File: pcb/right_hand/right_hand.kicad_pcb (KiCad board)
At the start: 2 copper layers, 160 x 110 mm, 113 parts, among them J0 UJ20-C-H-G-SMT-P16-TR, U0 SW_Push

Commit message: Update right hand metadata
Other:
- board text added: "Stenoswitch Right Hand v0.3"
- board text removed: "Stenoswitch Right Hand v0.2"
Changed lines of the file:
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@@
 	(title_block
 		(title "Stenoswitch Right Hand")
-		(date "2025-09-05")
-		(rev "v0.2")
+		(date "2025-10-20")
+		(rev "v0.3")
 		(company "https://github.com/Bennett-Petzold/stenoswitch")
 		(comment 1 "NO WARRANTY. See license.")
@@
 		(layer "Edge.Cuts")
 	)
-	(gr_text "Stenoswitch Right Hand v0.2"
+	(gr_text "Stenoswitch Right Hand v0.3"
 		(at 184.2 57.6 0)
 		(layer "F.SilkS")
@@
 		)
 	)
-	(gr_text "Stenoswitch Right Hand v0.2"
+	(gr_text "Stenoswitch Right Hand v0.3"
 		(at 83.8 143.2 0)
 		(layer "F.SilkS")
@@
 		)
 	)
-	(gr_text "Stenoswitch Right Hand v0.2"
+	(gr_text "Stenoswitch Right Hand v0.3"
 		(at 111.35 145.32 0)
 		(layer "B.SilkS")
@@
 		)
 	)
-	(gr_text "Stenoswitch Right Hand v0.2"
+	(gr_text "Stenoswitch Right Hand v0.3"
 		(at 228.2 60.8 0)
 		(layer "B.SilkS")

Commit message: Readjust positive data ESD
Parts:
- moved CR1 4.31 mm to (73.6, 130.7)
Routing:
- net GND: vias 60 -> 59
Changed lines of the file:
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@@
 	(footprint "ultra_librarian_footprints:SOT5x3_DYA_TEX"
 		(layer "B.Cu")
-		(at 70.6 127.5493 -90)
+		(at 73.6 130.6507 -90)
 		(tags "ESD321DYAR ")
 		(property "Reference" "CR1"
@@
 			(polygon
 				(pts
-					(xy 70.2317 127.1556) (xy 70.2317 127.943) (xy 70.9683 127.943) (xy 70.9683 127.1556)
+					(xy 73.2317 130.257) (xy 73.2317 131.0444) (xy 73.9683 131.0444) (xy 73.9683 130.257)
 				)
 			)
@@
 	)
 	(via
-		(at 75.6 38.6)
-		(size 1.2)
-		(drill 0.6)
-		(layers "F.Cu" "B.Cu")
-		(free yes)
-		(net 15)
-	)
-	(via
 		(at 151.2 98.4)
 		(size 1.2)
@@
 	)
 	(segment
-		(start 70.6 126.8)
-		(end 70.5 126.7)
+		(start 73.6 129.9014)
+		(end 73.5 129.8014)
 		(width 0.5)
 		(layer "B.Cu")
@@
 	)
 	(segment
-		(start 70.5 126.7)
-		(end 70.5 125.94994)
+		(start 73.5 129.8014)
+		(end 73.5 129.05134)
 		(width 0.5)
 		(layer "B.Cu")
@@
 			)
 		)
+	)
+	(zone
+		(net 0)
+		(net_name "")
+		(layer "B.Cu")
+		(hatch edge 0.5)
+		(connect_pads
+			(clearance 0)
+		)
+		(min_thickness 0.25)
+		(filled_areas_thickness no)
+		(keepout
+			(tracks allowed)
+			(vias allowed)
+			(pads allowed)
+			(copperpour not_allowed)
+			(footprints allowed)
+		)
+		(placement
+			(enabled no)
+			(sheetname "")
+		)
+		(fill
+			(thermal_gap 0.5)
+			(thermal_bridge_width 0.5)
+		)
+		(polygon
+			(pts
+				(xy 100.4 38.8) (xy 100.4 37.2) (xy 98.8 37.2) (xy 98.8 38.6)
+			)
+		)

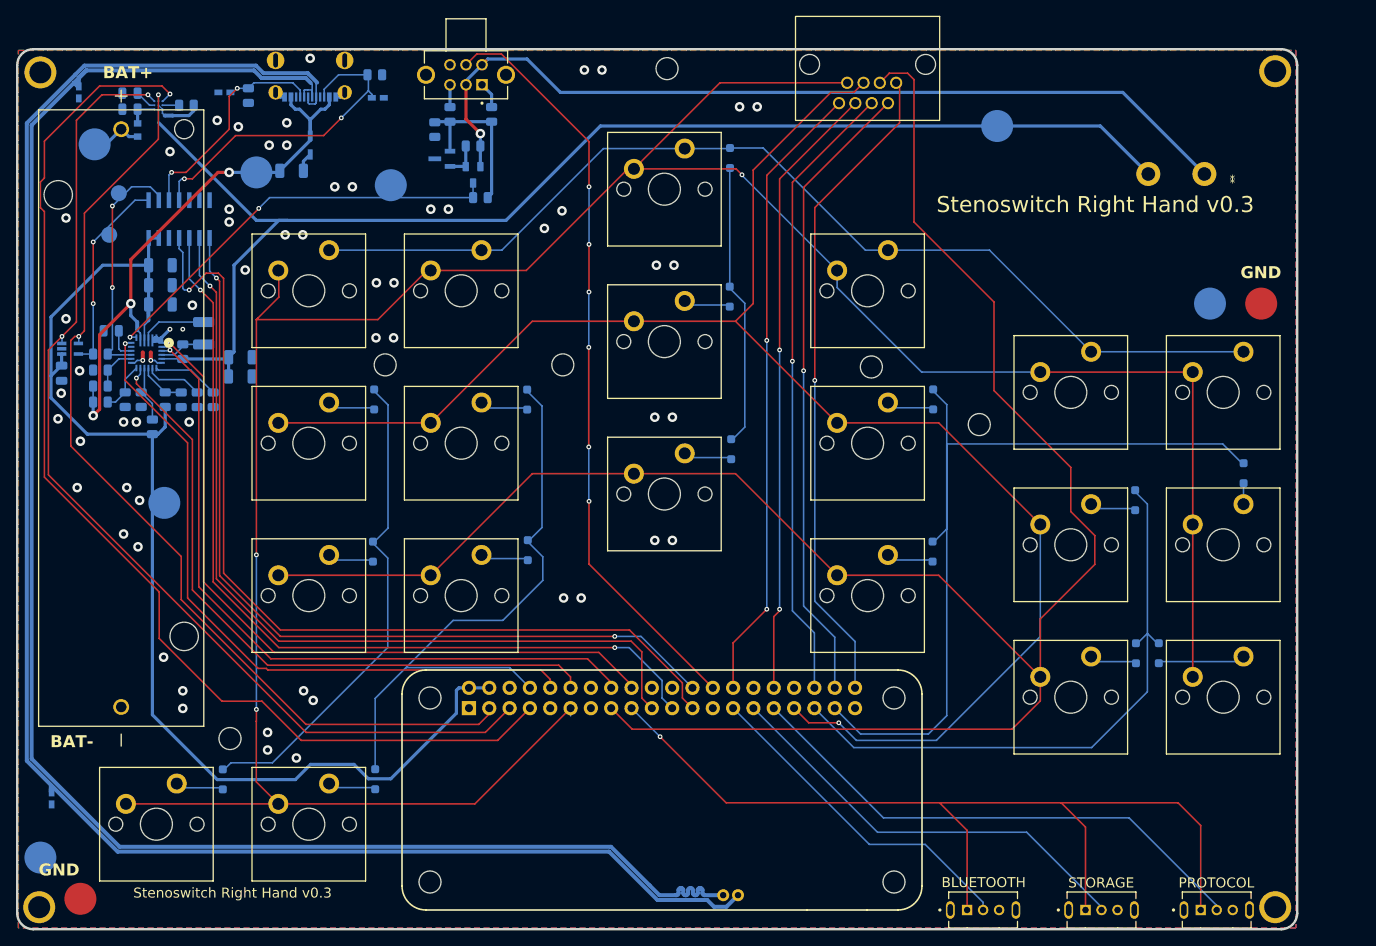
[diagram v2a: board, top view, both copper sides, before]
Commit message: Add more ESD protection
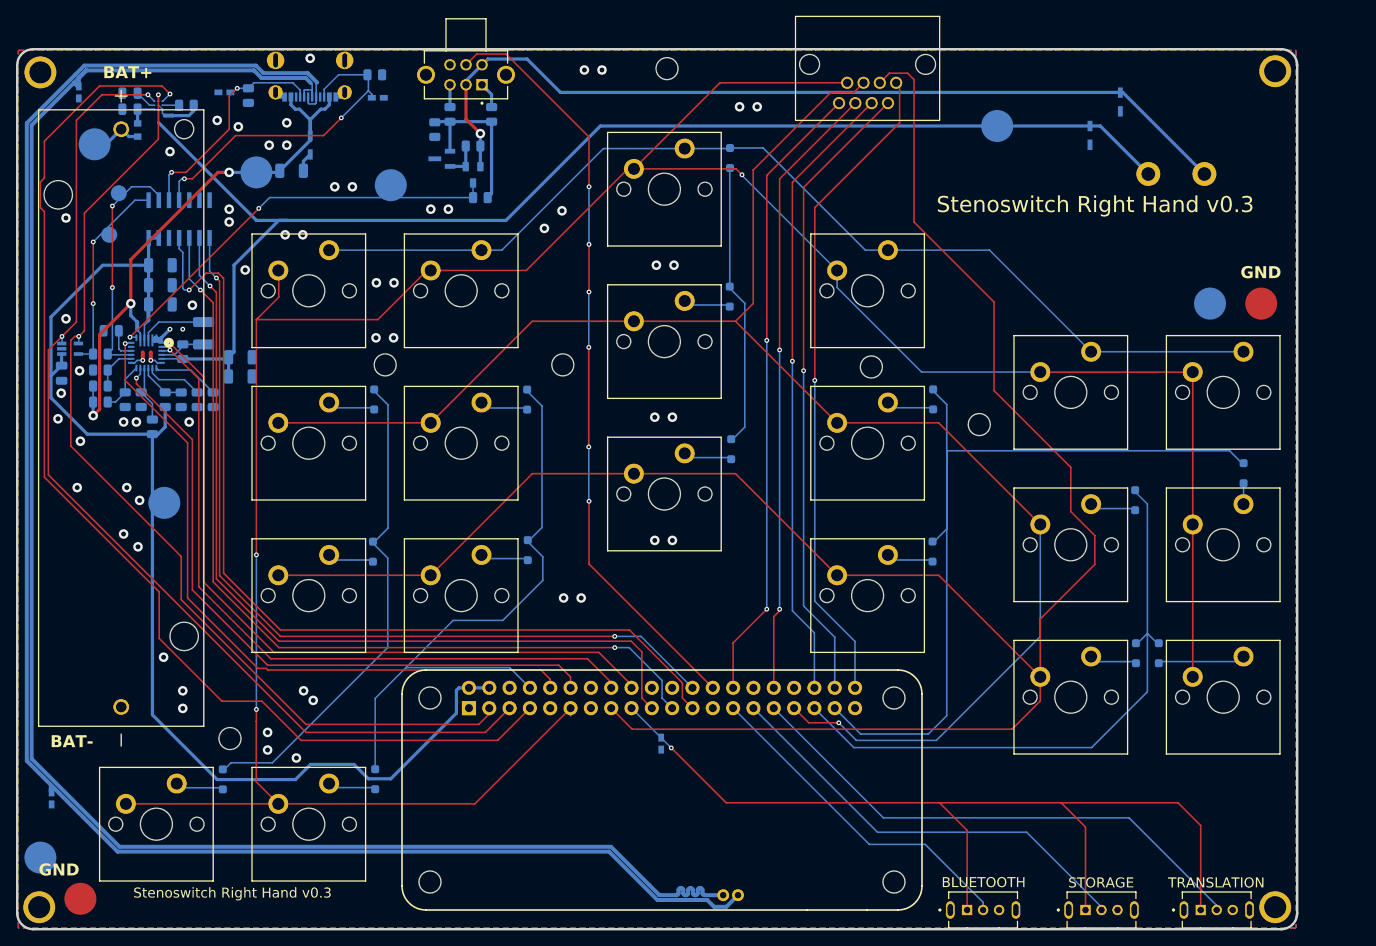
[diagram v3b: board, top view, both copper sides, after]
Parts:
- added CR5: ESD321DYAR, ultra_librarian_footprints:SOT5x3_DYA_TEX, B.Cu at (149.8, 123.8)
- added TSD05: TSD05DYFR, ultra_librarian_footprints:TVS_SOD2_DYF_TEX, B.Cu at (207.2, 43.6)
- added TSD05: TSD05DYFR, ultra_librarian_footprints:TVS_SOD2_DYF_TEX, B.Cu at (203.4, 47.8)
- CR1, CR4: value ESD321 -> ESD321DYAR
- CR2: value TSD05 -> TSD05DYFR
- C_{SYS}1: value 22uF(3) -> 22uF
- RFB_{H}0: value 31.6K -> 31.6k
- RLIM_{H}0: value 10K -> 10k
- RLIM_{L}0: value MCP40D19T -> MCP40D19T-104E_LT
- RNTC_{L}0: value 10K(2) -> 10k
- RREG_{H}0: value 15K -> 15k
- RWIN_{H}0: value 21.5K -> 21.5k
- RWIN_{L}0: value 5.1K -> 5.1k
- R_{ISET}0: value 73.2K -> 73.2k
- R_{OLIM}0: value 590K -> 590k
- R_{Store}0: value 8.06K -> 8.06k
- renumbered BAT_STORE to STORE_EN0, PROTOCOL to TRANSLATION
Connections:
- BLUETOOTH pad SH1: (no net) -> GND
- BLUETOOTH pad SH2: (no net) -> GND
- STORAGE pad SH1: (no net) -> GND
- STORAGE pad SH2: (no net) -> GND
- STORE_EN0 pad 6: unconnected-(STORE_EN0-Pad6) -> GND
- TRANSLATION pad SH1: (no net) -> GND
- TRANSLATION pad SH2: (no net) -> GND
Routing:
- net /Control/Right_Columns1: track 108.9 -> 107.7 mm
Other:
- board text added: "ESD321"
- board text added: "Fuse"

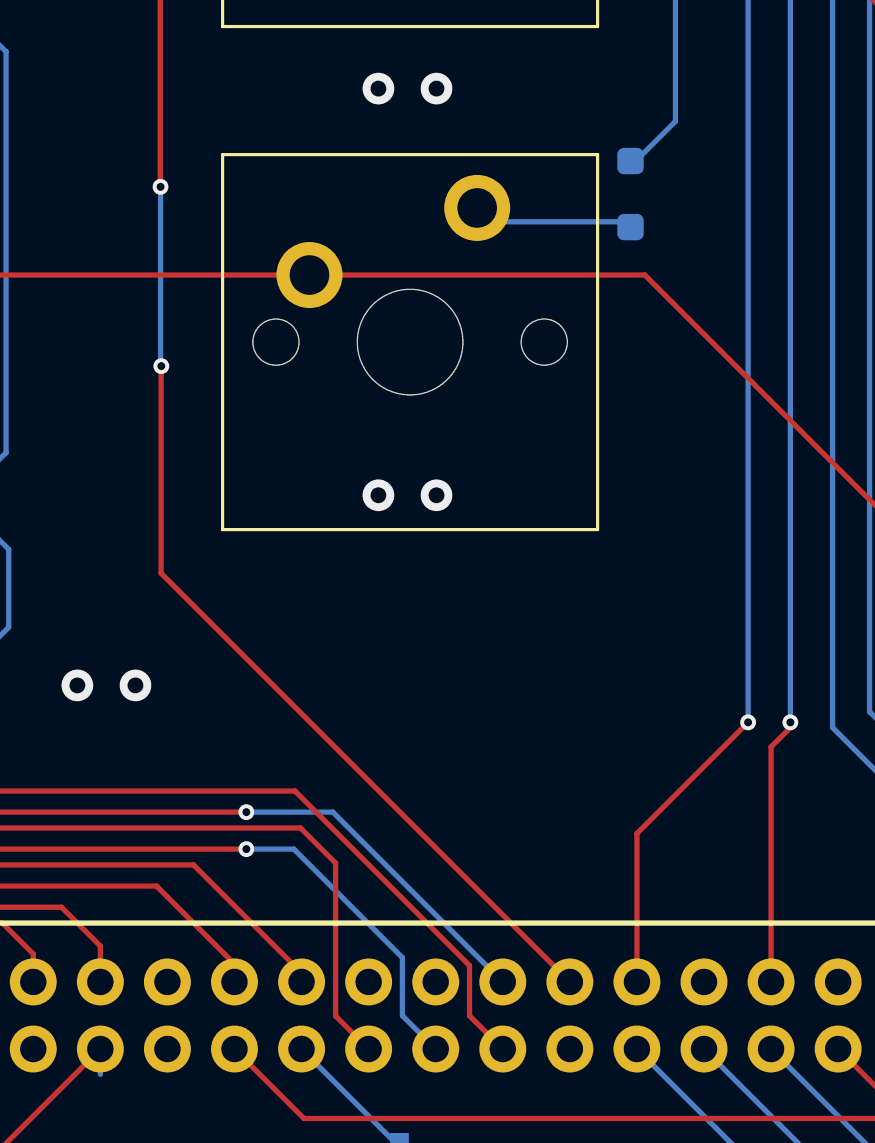
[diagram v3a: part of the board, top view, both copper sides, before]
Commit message: Connect right_columns 2 to RPi
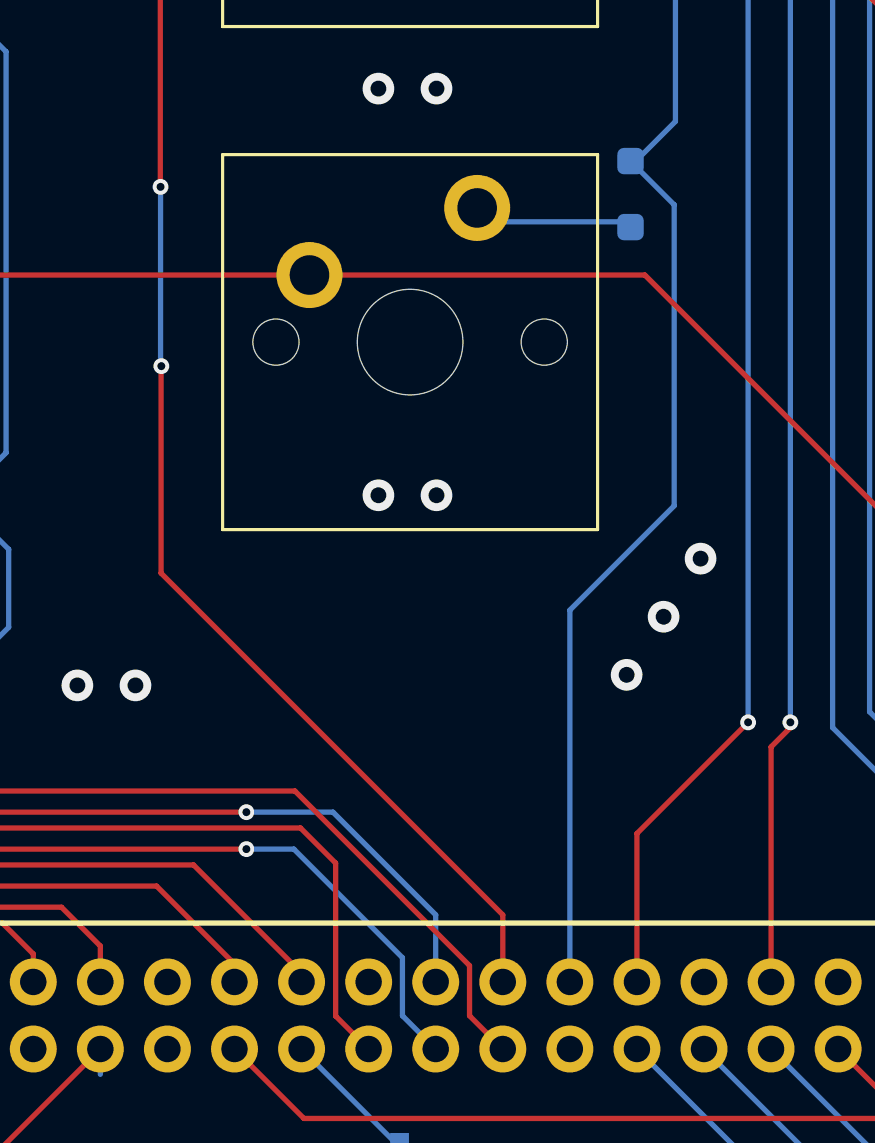
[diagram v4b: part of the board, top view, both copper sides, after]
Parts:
- BAT_MIN0: value DMG2305 -> DMG2305UX-7
- CR3: value ESD321 -> ESD321DYAR
- VBAT_PASS0: value TLV431 -> TLV431BIDBZR
- renumbered TSD05 to CR6, TSD05 to CR7
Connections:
- A1 pad 22: unconnected-(A1-GP25-Pad22) -> /Control/CS_{CURRENT}
- A1 pad 24: /Control/CS_{CURRENT} -> /Control/STORE_{ON}
- A1 pad 26: /Control/STORE_{ON} -> /Control/Right_Columns2
- BLUETOOTH pad SH1: GND -> (no net)
- BLUETOOTH pad SH2: GND -> (no net)
- STORAGE pad SH1: GND -> (no net)
- STORAGE pad SH2: GND -> (no net)
- TRANSLATION pad SH1: GND -> (no net)
- TRANSLATION pad SH2: GND -> (no net)
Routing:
- net /Control/Right_Columns2: track 35.4 -> 68.8 mm
- net /Control/CS_{CURRENT}: track 107.6 -> 106.6 mm
- net /Control/STORE_{ON}: track 95.5 -> 94.5 mm
- net GND: vias 59 -> 62

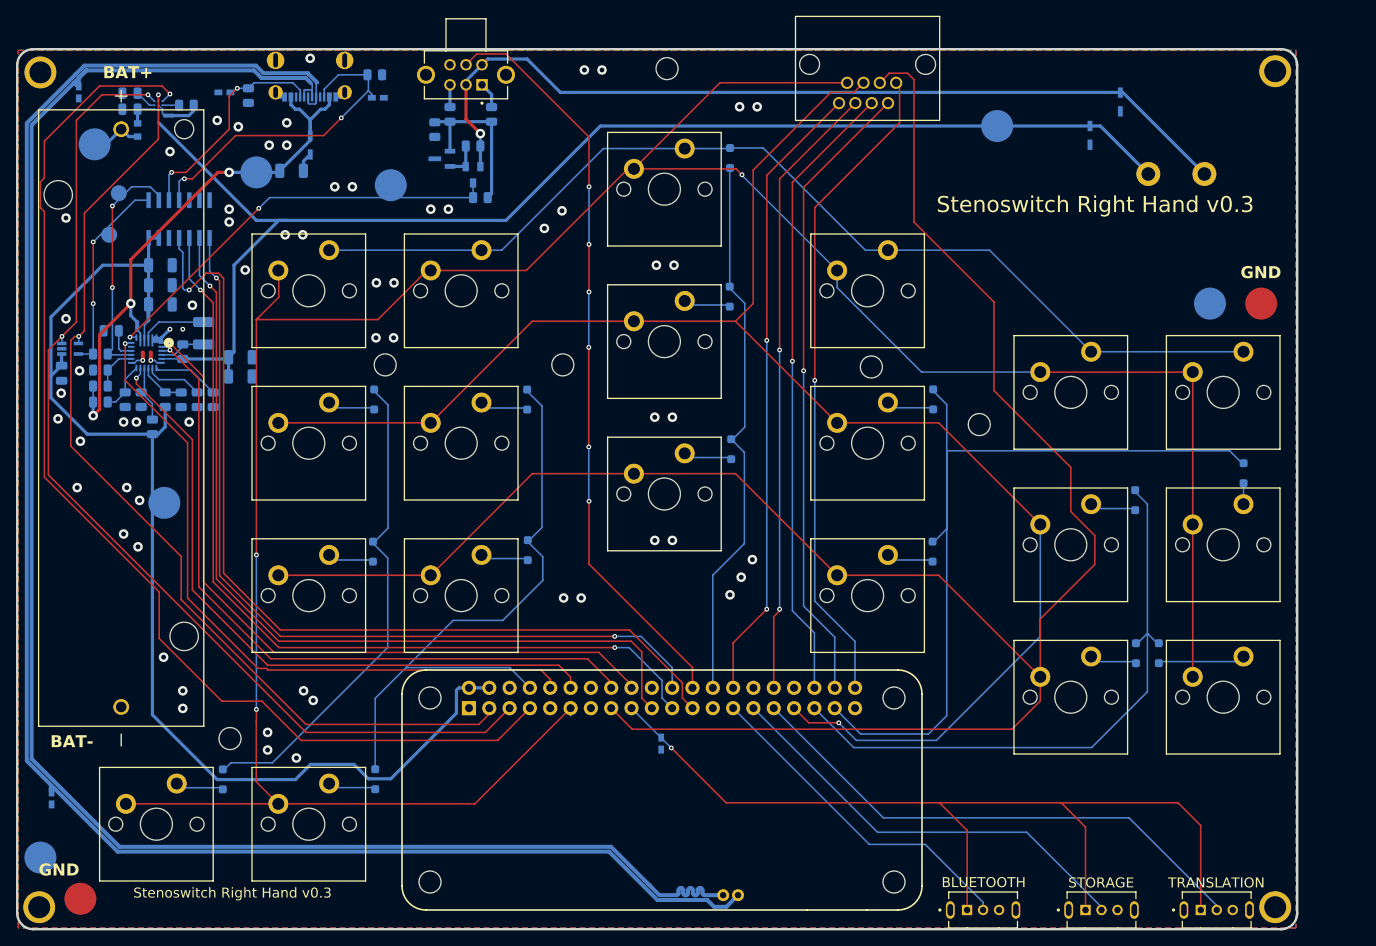
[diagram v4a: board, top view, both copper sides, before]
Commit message: Ground right hand through holes
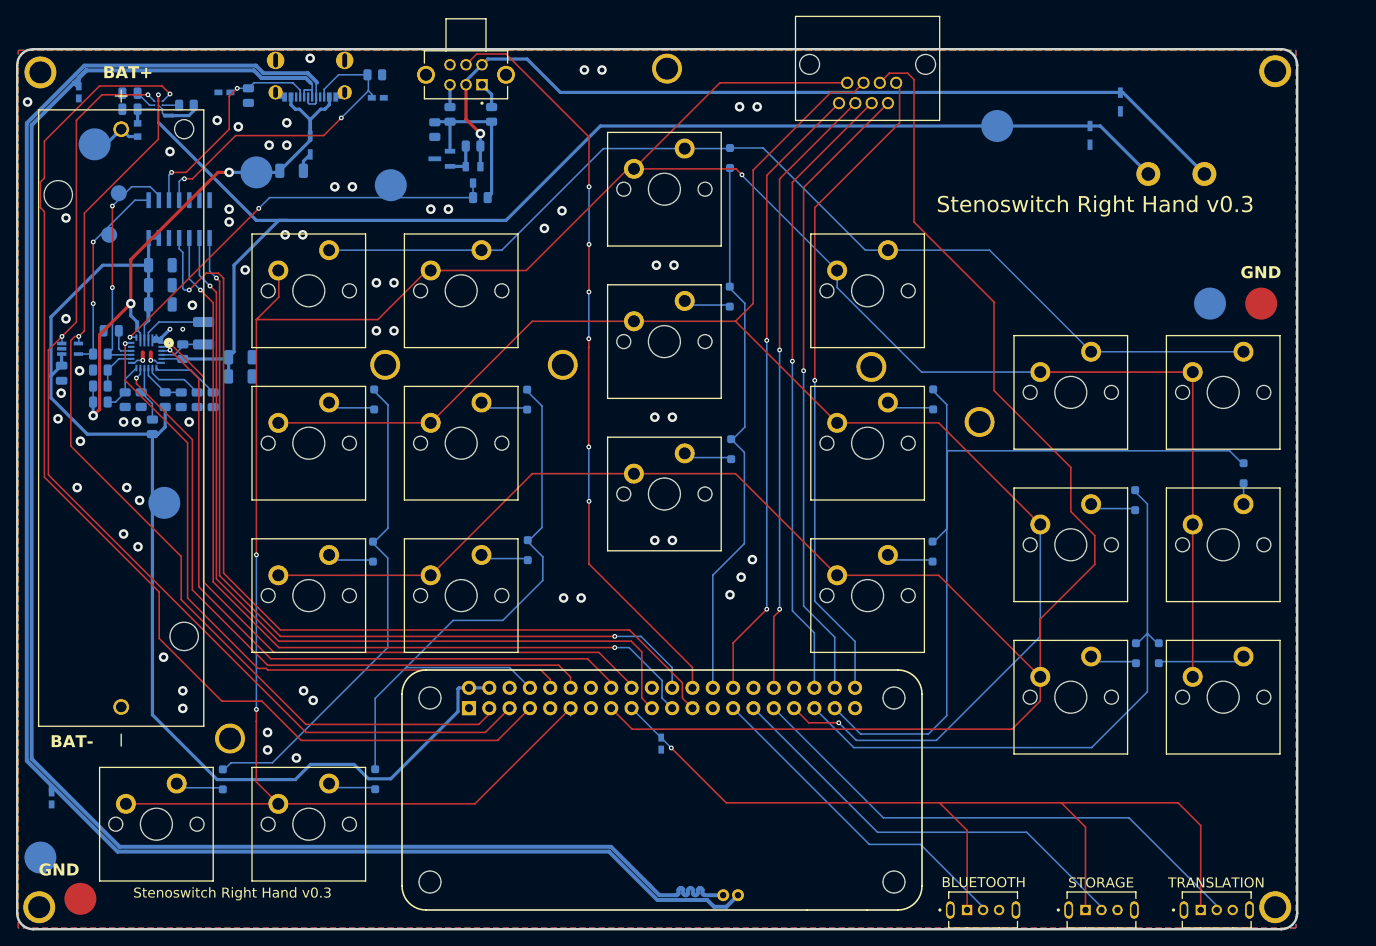
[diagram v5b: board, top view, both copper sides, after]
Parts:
- moved ? 0.32 mm to (189.6, 83.6)
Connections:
- ? pad : (no net) -> GND (x10)
- BLUETOOTH pad SH1: (no net) -> GND
- BLUETOOTH pad SH2: (no net) -> GND
- STORAGE pad SH1: (no net) -> GND
- STORAGE pad SH2: (no net) -> GND
- STORE_EN0 pad S1: (no net) -> GND
- STORE_EN0 pad S2: (no net) -> GND
- TRANSLATION pad SH1: (no net) -> GND
- TRANSLATION pad SH2: (no net) -> GND
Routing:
- net GND: vias 62 -> 63
